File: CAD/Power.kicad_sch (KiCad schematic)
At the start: 89 parts, among them U10 AOZ1284, U18 AP7330-W5-7, U24 LM70860RRXR, U4 AP7361C-33E-13

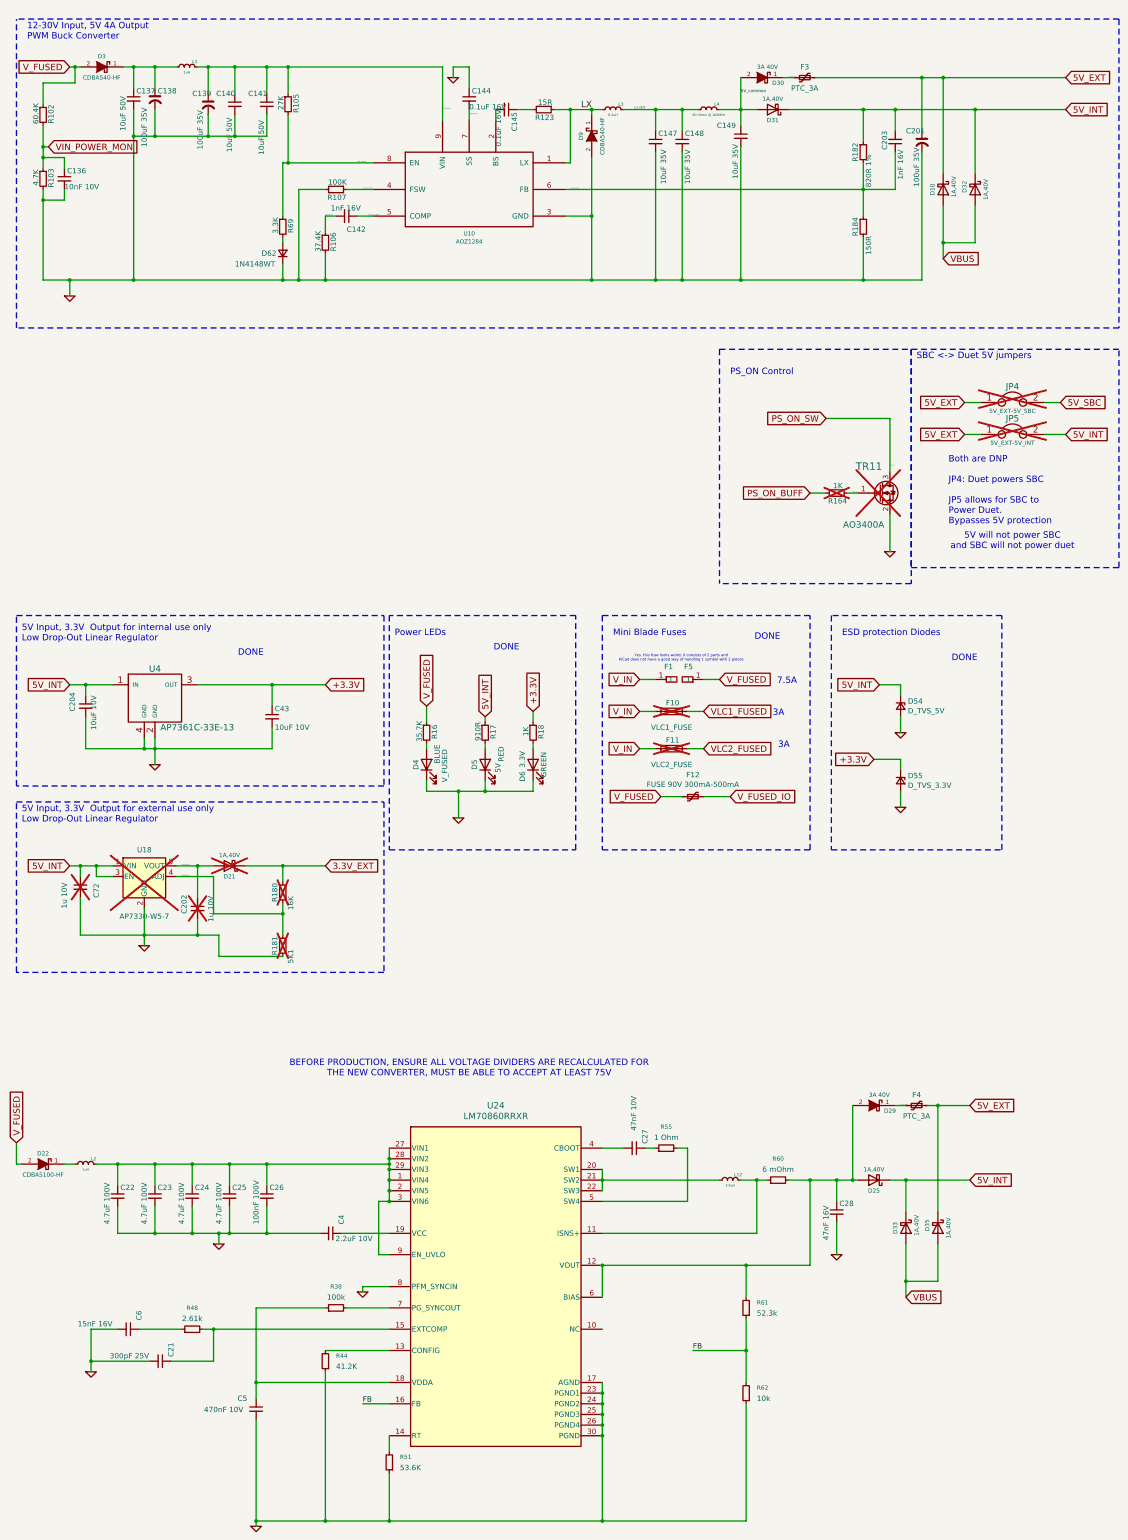
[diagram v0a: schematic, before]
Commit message: LM70860 Schematic: DONE
Schematic Finished, physical layout next
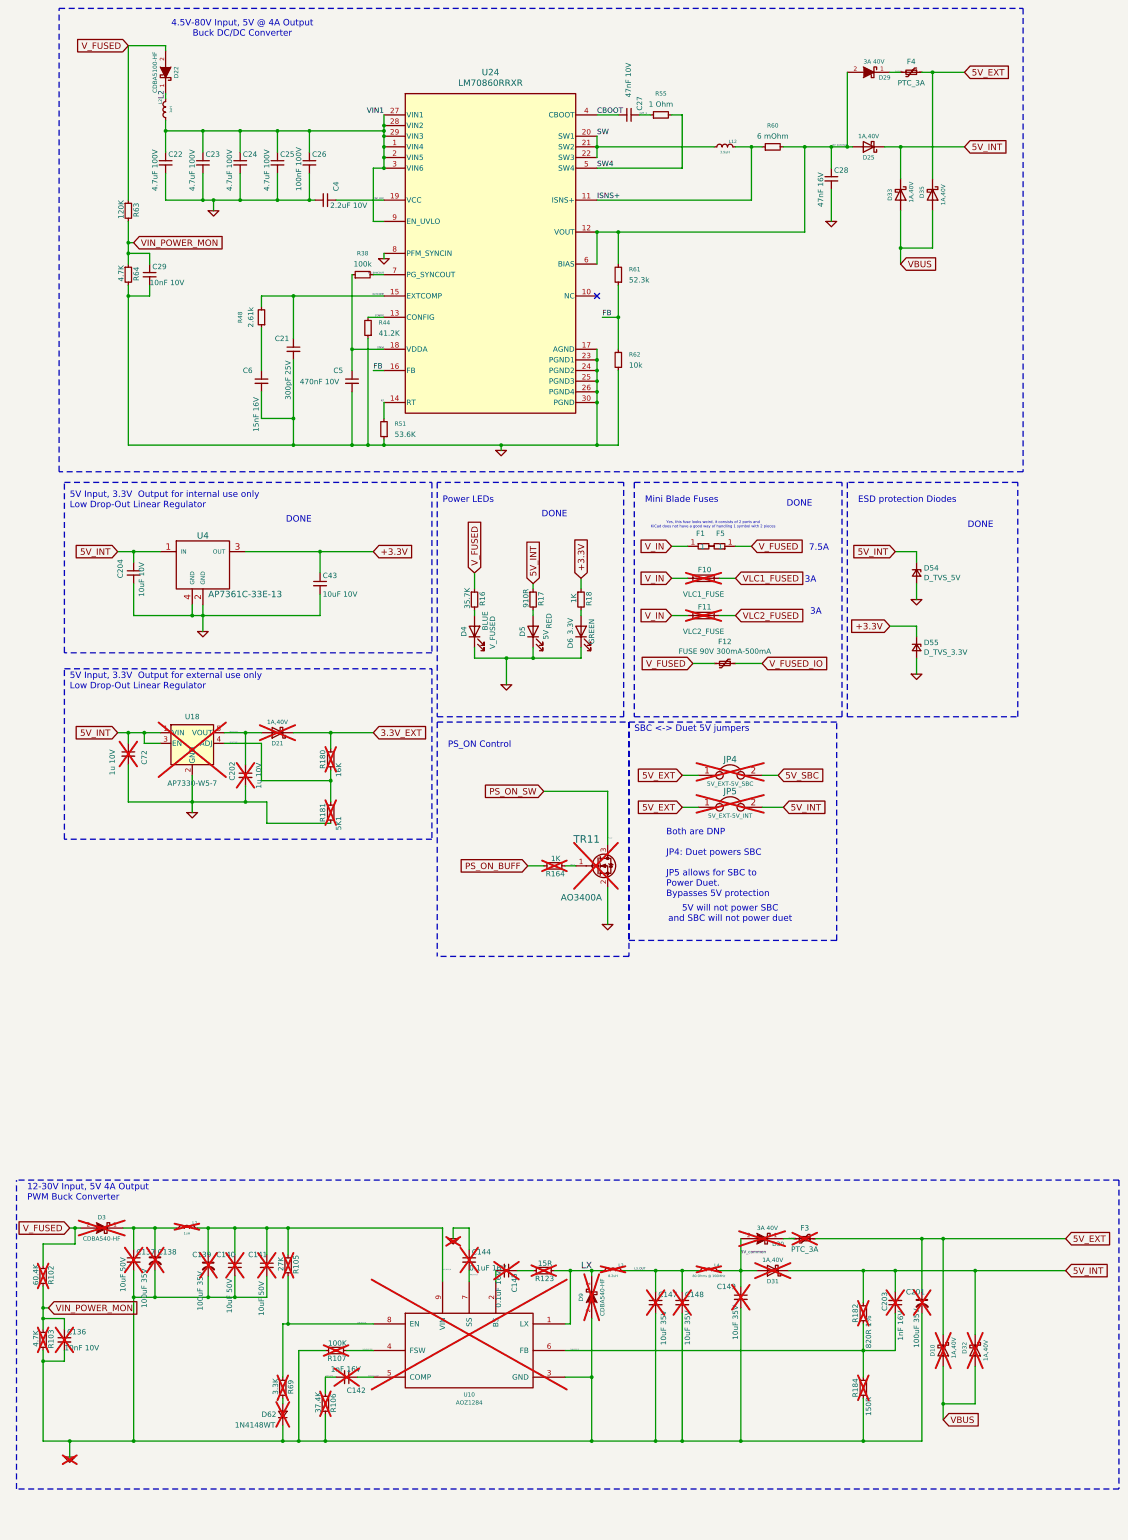
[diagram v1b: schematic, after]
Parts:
- added C29: 10nF 10V, Capacitor_SMD:C_0402_1005Metric, symbol Device:C_Small
- added R63: 120K, Resistor_SMD:R_0805_2012Metric, symbol Device:R_Small
- added R64: 4.7K, Resistor_SMD:R_0402_1005Metric, symbol Device:R_Small
- C136, C137, C138, C139, C140, C141, C142, C144, C145, C147, C148, C149, C201, C203, D10, D3, D30, D31, D32, D62, D9, F3, L1, L3, L4, R102, R103, R105, R106, R107, R123, R182, R184, R69, U10: now not fitted; now left out of the parts list
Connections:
- net GND: now also C29.2, R64.2
- net VIN_POWER_MON: now also C29.1, R63.2, R64.1
- net V_FUSED: now also R63.1
- net VIN1: now reaches C22.1, C23.1, C24.1, C25.1, C26.1, U24.1 (VIN4), U24.2 (VIN5), U24.27 (VIN1), U24.28 (VIN2), U24.29 (VIN3), U24.3 (VIN6), U24.9 (EN_UVLO)
- net VIN1: now also L2.2 (B); no longer L2.1 (A)
- net C27_1: now reaches C27.1, R55.1
- net SW4: now reaches R55.2, U24.5 (SW4)
- net 5V_Common: now reaches C28.1, D25.2 (A), D29.2 (A), R60.2, R61.2, U24.12 (VOUT), U24.6 (BIAS)
- net CAP_VCC: now reaches C4.1, U24.19 (VCC)
- net CBOOT: now reaches C27.2, U24.4 (CBOOT)
- net RT: now reaches R51.2, U24.14 (RT)
- net L2: now reaches D22.1 (K)
- net L2: now also L2.1 (A); no longer L2.2 (B)
- net VDDA: now reaches C5.1, R38.1, U24.18 (VDDA)
- net EXTCOMP: now reaches C21.1, R48.2, U24.15 (EXTCOMP)
- net ISNS+: now reaches L12.1 (A), R60.1, U24.11 (ISNS+)
- net SW: now reaches L12.2 (B), U24.20 (SW1), U24.21 (SW2), U24.22 (SW3)
- net CONFIG: now reaches R44.2, U24.13 (CONFIG)
- net PG_SYNCOUT: now reaches R38.2, U24.7 (PG_SYNCOUT)
- no-connect marks 0 -> 1
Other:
- note added: "4.5V-80V Input, 5V @ 4A Output Buck DC/DC Converter"
- note removed: "BEFORE PRODUCTION, ENSURE ALL VOLTAGE DIVIDERS ARE RECALCULATED FOR THE NEW CONVERTER, MUST BE ABLE TO ACCEPT AT LEAST 75V"
- moved on the sheet: C202, C204, C21, C22, C23, C24, C25, C26, C27, C28, C4, C43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

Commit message: PCB Layout Started
Current sensing, PG_SYNCOUT to VDDA to GND, CBOOT, Feedback are done! Fuse holder is laid out, but now we need a new power terminal, most likely changing to 250-502/000-006 from WAGO.
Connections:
- net C6_1: now reaches C6.1, R48.1
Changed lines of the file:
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@@
+		)
+	)
+	(label "C6_1"
+		(at 76.2 100.33 90)
+		(effects
+			(font
+				(size 1.27 1.27)
+			)
+			(justify left bottom)
 		)
 	)

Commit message: PCB Done
As far as I am aware, everything is done, still needs to be run through JLCDFM.
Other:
- note added: "Yes, this fuse looks weird, it consists of 2 parts and KiCad does not have a good way of handling 1 symbol with 2 pieces Fuse holder for 1/4"x1 1/4" (6.38mmx35mm) Ceramic (or glass?) fuses"
- note removed: "Yes, this fuse looks weird, it consists of 2 parts and KiCad does not have a good way of handling 1 symbol with 2 pieces"
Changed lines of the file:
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@@
 		)
 	)
-	(text "Yes, this fuse looks weird, it consists of 2 parts and\nKiCad does not have a good way of handling 1 symbol with 2 pieces"
+	(text "Yes, this fuse looks weird, it consists of 2 parts and\nKiCad does not have a good way of handling 1 symbol with 2 pieces\nFuse holder for 1/4\"x1 1/4\" (6.38mmx35mm) Ceramic (or glass?) fuses"
 		(exclude_from_sim no)
-		(at 183.896 137.16 0)
+		(at 183.896 136.144 0)
 		(effects
 			(font

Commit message: QOL
Added a buttload of 3d models, 3d model of board is now usable. Also saved a lot of missing symbols and footprints, which are available in the 3DPotter Library.
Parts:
- F4: footprint Fuse:Fuse_1812_4532Metric -> 3DPotter:Fuse_1812_4532Metric
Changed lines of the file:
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@@
 			)
 		)
-		(property "Footprint" "Fuse:Fuse_1812_4532Metric"
+		(property "Footprint" "3DPotter:Fuse_1812_4532Metric"
 			(at 226.06 30.48 0)
 			(effects

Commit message: Misc Changes
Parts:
- D22: symbol Duet3:CDBA540 -> 3DPotter:CDBA5100
- L2: footprint Inductor_SMD:L_1210_3225Metric -> Inductor_SMD:L_1008_2520Metric
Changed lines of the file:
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@@
 			)
 		)
-		(property "Footprint" "Inductor_SMD:L_1210_3225Metric"
+		(property "Footprint" "Inductor_SMD:L_1008_2520Metric"
 			(at 53.34 38.1 0)
 			(effects
@@
 	)
 	(symbol
-		(lib_id "Duet3:CDBA540")
+		(lib_id "3DPotter:CDBA5100")
 		(at 53.34 29.21 270)
 		(unit 1)

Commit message: remove step gate pull down resistor
change D22 to the correct manufacturer part number
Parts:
- D22: value CDBA5100-HF -> ACDBC5100-HF; Part Number CDBA5100-HF -> ACDBC5100-HF
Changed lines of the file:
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@@
 			)
 		)
-		(property "Value" "CDBA5100-HF"
+		(property "Value" "ACDBC5100-HF"
 			(at 50.8 29.21 0)
 			(effects
@@
 			)
 		)
-		(property "Part Number" "CDBA5100-HF"
+		(property "Part Number" "ACDBC5100-HF"
 			(at 53.34 29.21 0)
 			(effects
